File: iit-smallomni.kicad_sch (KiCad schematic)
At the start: 82 parts, among them J1 Battery, J10 DC-Motor, J2 HC_SR04, J3 HC_SR04, J4 HC_SR04, J5 DC-Motor, J6 DC-Motor, J7 DC-Motor, J8 DC-Motor, J9 DC-Motor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

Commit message: Change reset capacitor to 10uF
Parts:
- C1: value 10n -> 10u
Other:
- note added: "10uF to auto-reset when programming"
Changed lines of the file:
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@@
 		)
 	)
+	(text "10uF to auto-reset\nwhen programming"
+		(exclude_from_sim no)
+		(at 172.466 31.75 0)
+		(effects
+			(font
+				(size 1.27 1.27)
+			)
+		)
+	)
 	(text "MPU-9250 IMU"
 		(exclude_from_sim no)
@@
 			)
 		)
-		(property "Value" "10n"
+		(property "Value" "10u"
 			(at 173.99 44.45 0)
 			(effects

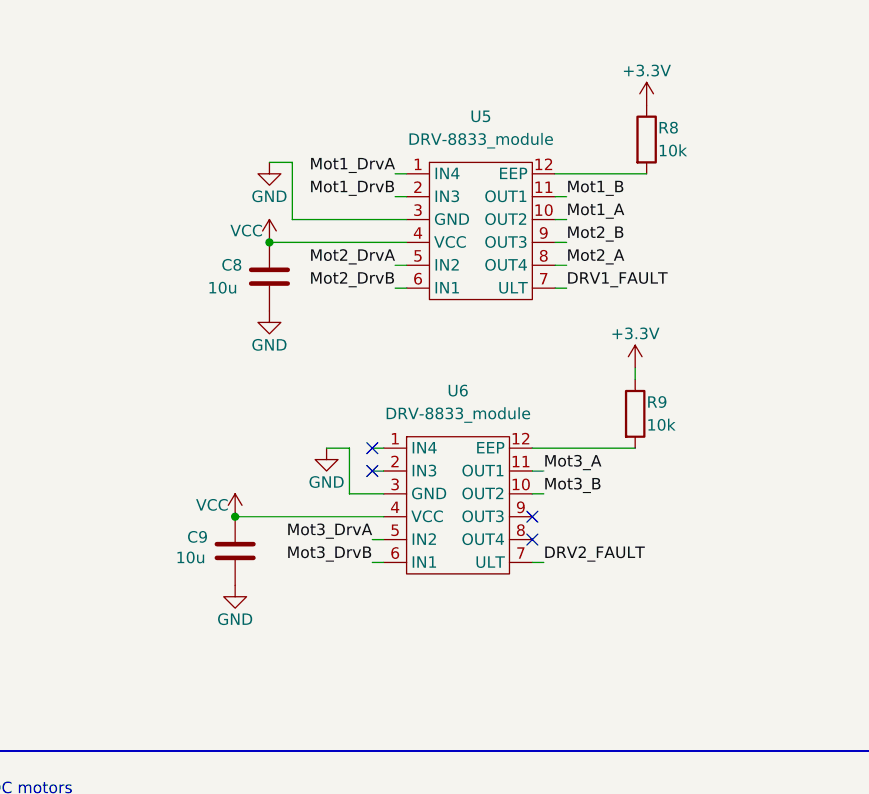
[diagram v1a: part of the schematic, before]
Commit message: Fix flipped DRV8833
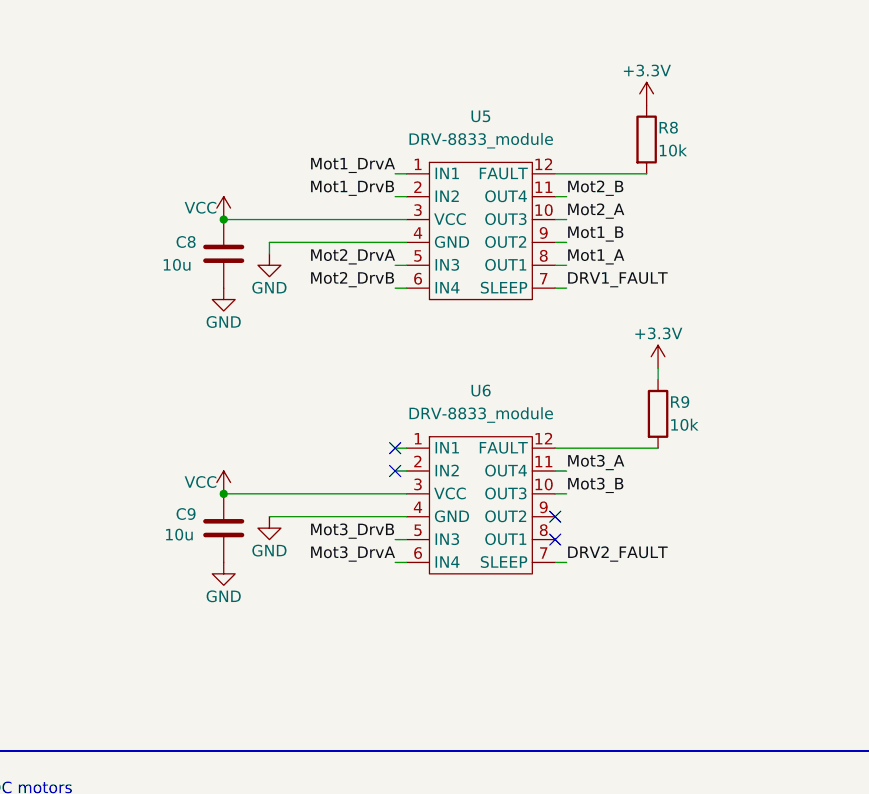
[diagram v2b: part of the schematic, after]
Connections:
- net GND: now also U5.4 (GND), U6.4 (GND); no longer U5.3 (GND), U6.3 (GND)
- net Mot1_A: now also U5.8 (OUT1); no longer U5.10 (OUT2)
- net Mot1_B: now also U5.9 (OUT2); no longer U5.11 (OUT1)
- net Mot2_A: now also U5.10 (OUT3); no longer U5.8 (OUT4)
- net Mot2_B: now also U5.11 (OUT4); no longer U5.9 (OUT3)
- net Mot3_DrvA: now also U6.6 (IN4); no longer U6.5 (IN2)
- net Mot3_DrvB: now also U6.5 (IN3); no longer U6.6 (IN1)
- net VCC: now also U5.3 (VCC), U6.3 (VCC); no longer U5.4 (VCC), U6.4 (VCC)
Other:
- moved on the sheet: C8, C9, R9, U6

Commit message: Fix flipped DSN-1504
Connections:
- net +5V: now also U2.4 (Output+); no longer U2.3 (Output+)
- net GND: now also U2.2 (Input-), U2.3 (Output-); no longer U2.1 (Input-), U2.4 (Output-)
- net Mot3_DrvA: now also U6.5 (IN3); no longer U6.6 (IN4)
- net Mot3_DrvB: now also U6.6 (IN4); no longer U6.5 (IN3)
- net at D1.1 (K): now also U2.1 (Input+); no longer U2.2 (Input+)
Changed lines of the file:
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@@
 	)
 	(label "Mot3_DrvB"
-		(at 351.79 80.01 180)
+		(at 351.79 82.55 180)
 		(fields_autoplaced yes)
 		(effects
@@
 	)
 	(label "Mot3_DrvA"
-		(at 351.79 82.55 180)
+		(at 351.79 80.01 180)
 		(fields_autoplaced yes)
 		(effects
@@
 		(lib_id "iit-smallomni:DSN-1504_module")
 		(at 90.17 26.67 0)
-		(mirror x)
 		(unit 1)
 		(exclude_from_sim no)
@@
 		(dnp no)
 		(property "Reference" "U2"
-			(at 90.17 22.606 0)
+			(at 90.17 22.86 0)
 			(effects
 				(font
@@
 		)
 		(property "Value" "DSN-1504_module"
-			(at 90.678 21.082 0)
+			(at 90.424 20.828 0)
 			(effects
 				(font
@@
 		)
 		(property "Footprint" "iit-smallomni:DSN1504_module"
-			(at 82.55 30.48 0)
+			(at 82.55 22.86 0)
 			(effects
 				(font
@@
 		)
 		(property "Datasheet" ""
-			(at 82.55 30.48 0)
+			(at 82.55 22.86 0)
 			(effects
 				(font

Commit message: Update Schottky diode footprint in design
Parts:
- D1: footprint Diode_SMD:D_0805_2012Metric_Pad1.15x1.40mm_HandSolder -> iit-smallomni:D_SOD-123FL
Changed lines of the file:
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@@
 			)
 		)
-		(property "Footprint" "Diode_SMD:D_0805_2012Metric_Pad1.15x1.40mm_HandSolder"
+		(property "Footprint" "iit-smallomni:D_SOD-123FL"
 			(at 73.66 25.4 0)
 			(effects

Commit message: Fix motor connector layout
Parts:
- J10, J8, J9: footprint iit-smallomni:motor -> iit-smallomni:legacy-motor
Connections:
- net +3.3V: now also J10.4 (Pin_4), J8.4 (Pin_4), J9.4 (Pin_4); no longer J10.5 (Pin_5), J8.5 (Pin_5), J9.5 (Pin_5)
- net GND: now also J10.3 (Pin_3), J8.3 (Pin_3), J9.3 (Pin_3); no longer J10.2 (Pin_2), J8.2 (Pin_2), J9.2 (Pin_2)
- net Mot1_B: now also J8.2 (Pin_2); no longer J8.6 (Pin_6)
- net Mot1_EncA: now also J8.5 (Pin_5); no longer J8.3 (Pin_3)
- net Mot1_EncB: now also J8.6 (Pin_6); no longer J8.4 (Pin_4)
- net Mot2_B: now also J9.2 (Pin_2); no longer J9.6 (Pin_6)
- net Mot2_EncA: now also J9.5 (Pin_5); no longer J9.3 (Pin_3)
- net Mot2_EncB: now also J9.6 (Pin_6); no longer J9.4 (Pin_4)
- net Mot3_B: now also J10.2 (Pin_2); no longer J10.6 (Pin_6)
- net Mot3_EncA: now also J10.5 (Pin_5); no longer J10.3 (Pin_3)
- net Mot3_EncB: now also J10.6 (Pin_6); no longer J10.4 (Pin_4)

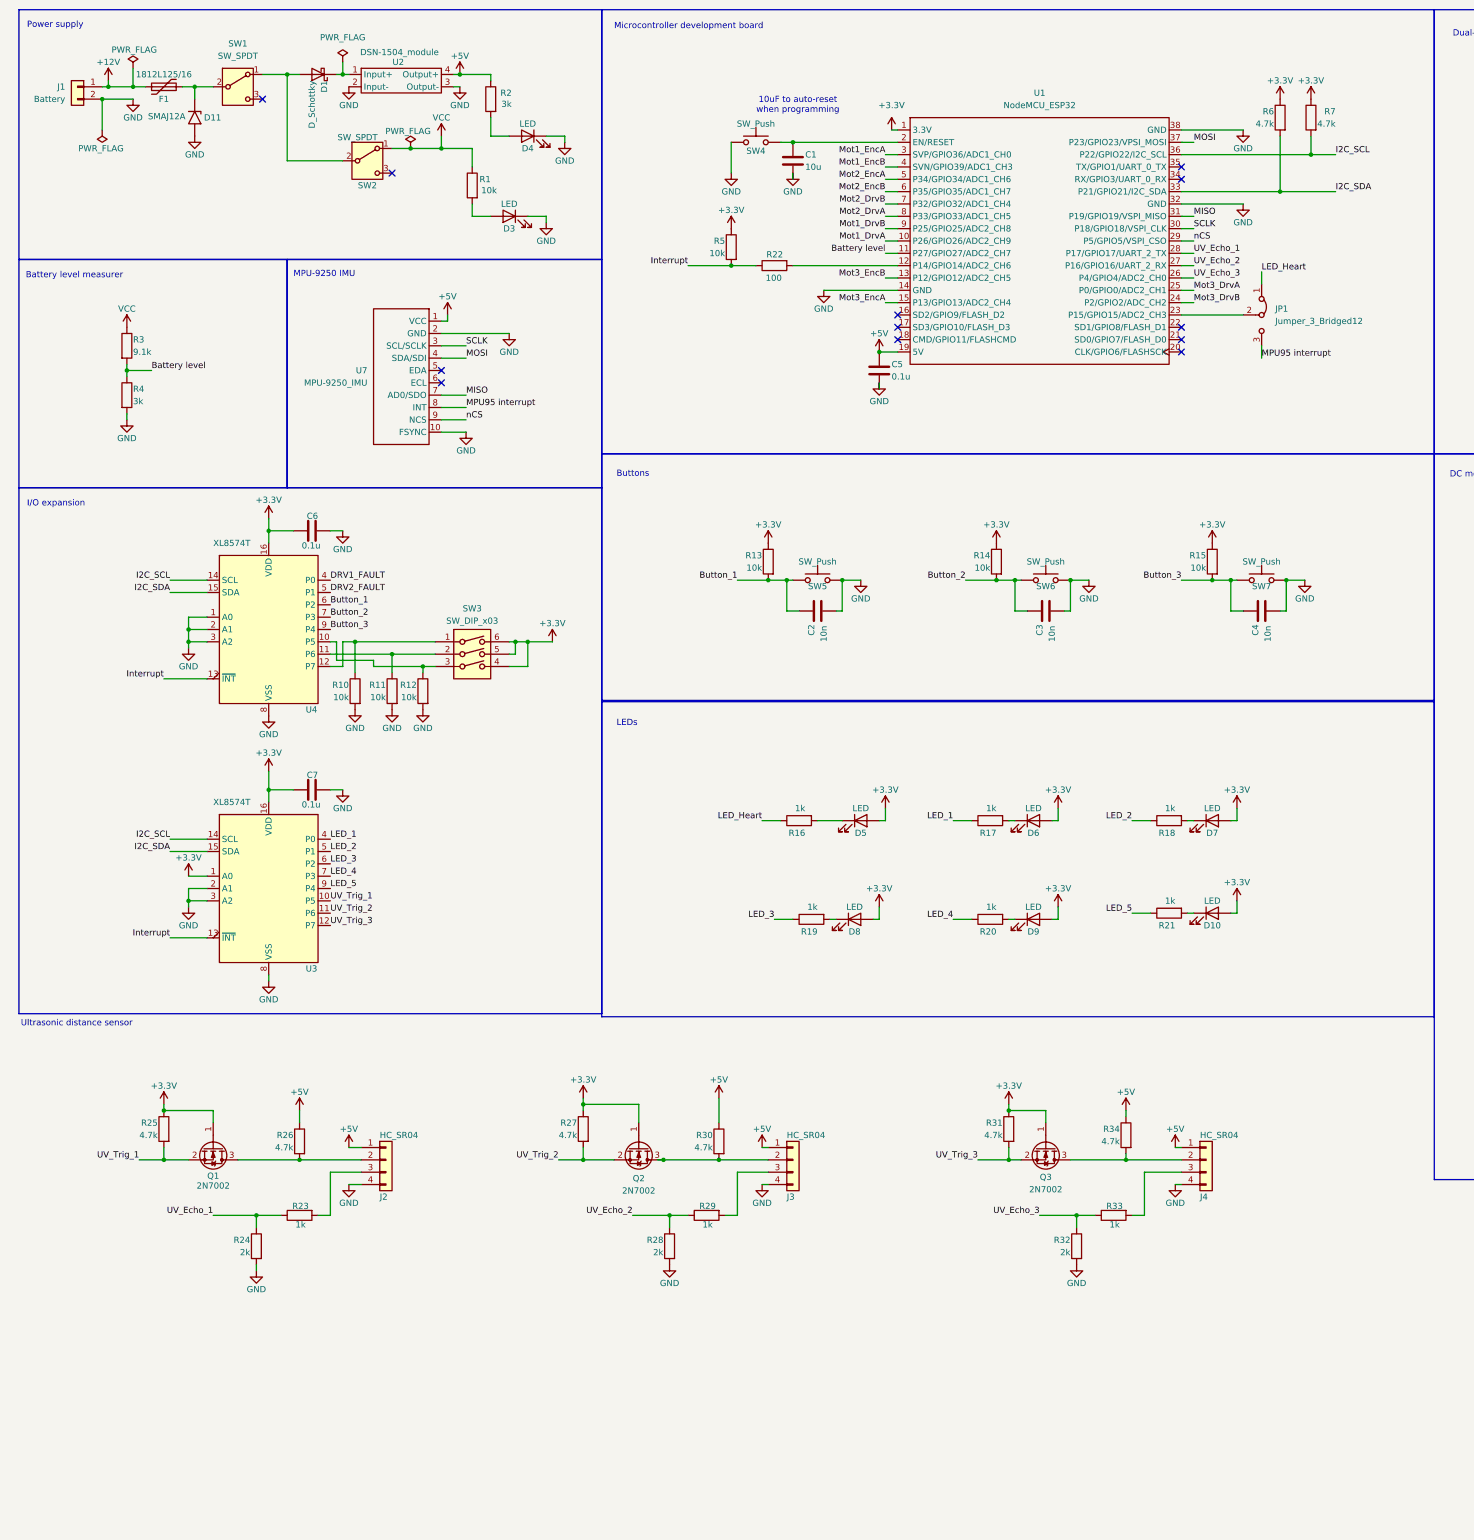
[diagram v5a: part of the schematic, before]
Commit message: JTAG, LiPo guard, Mounting hole
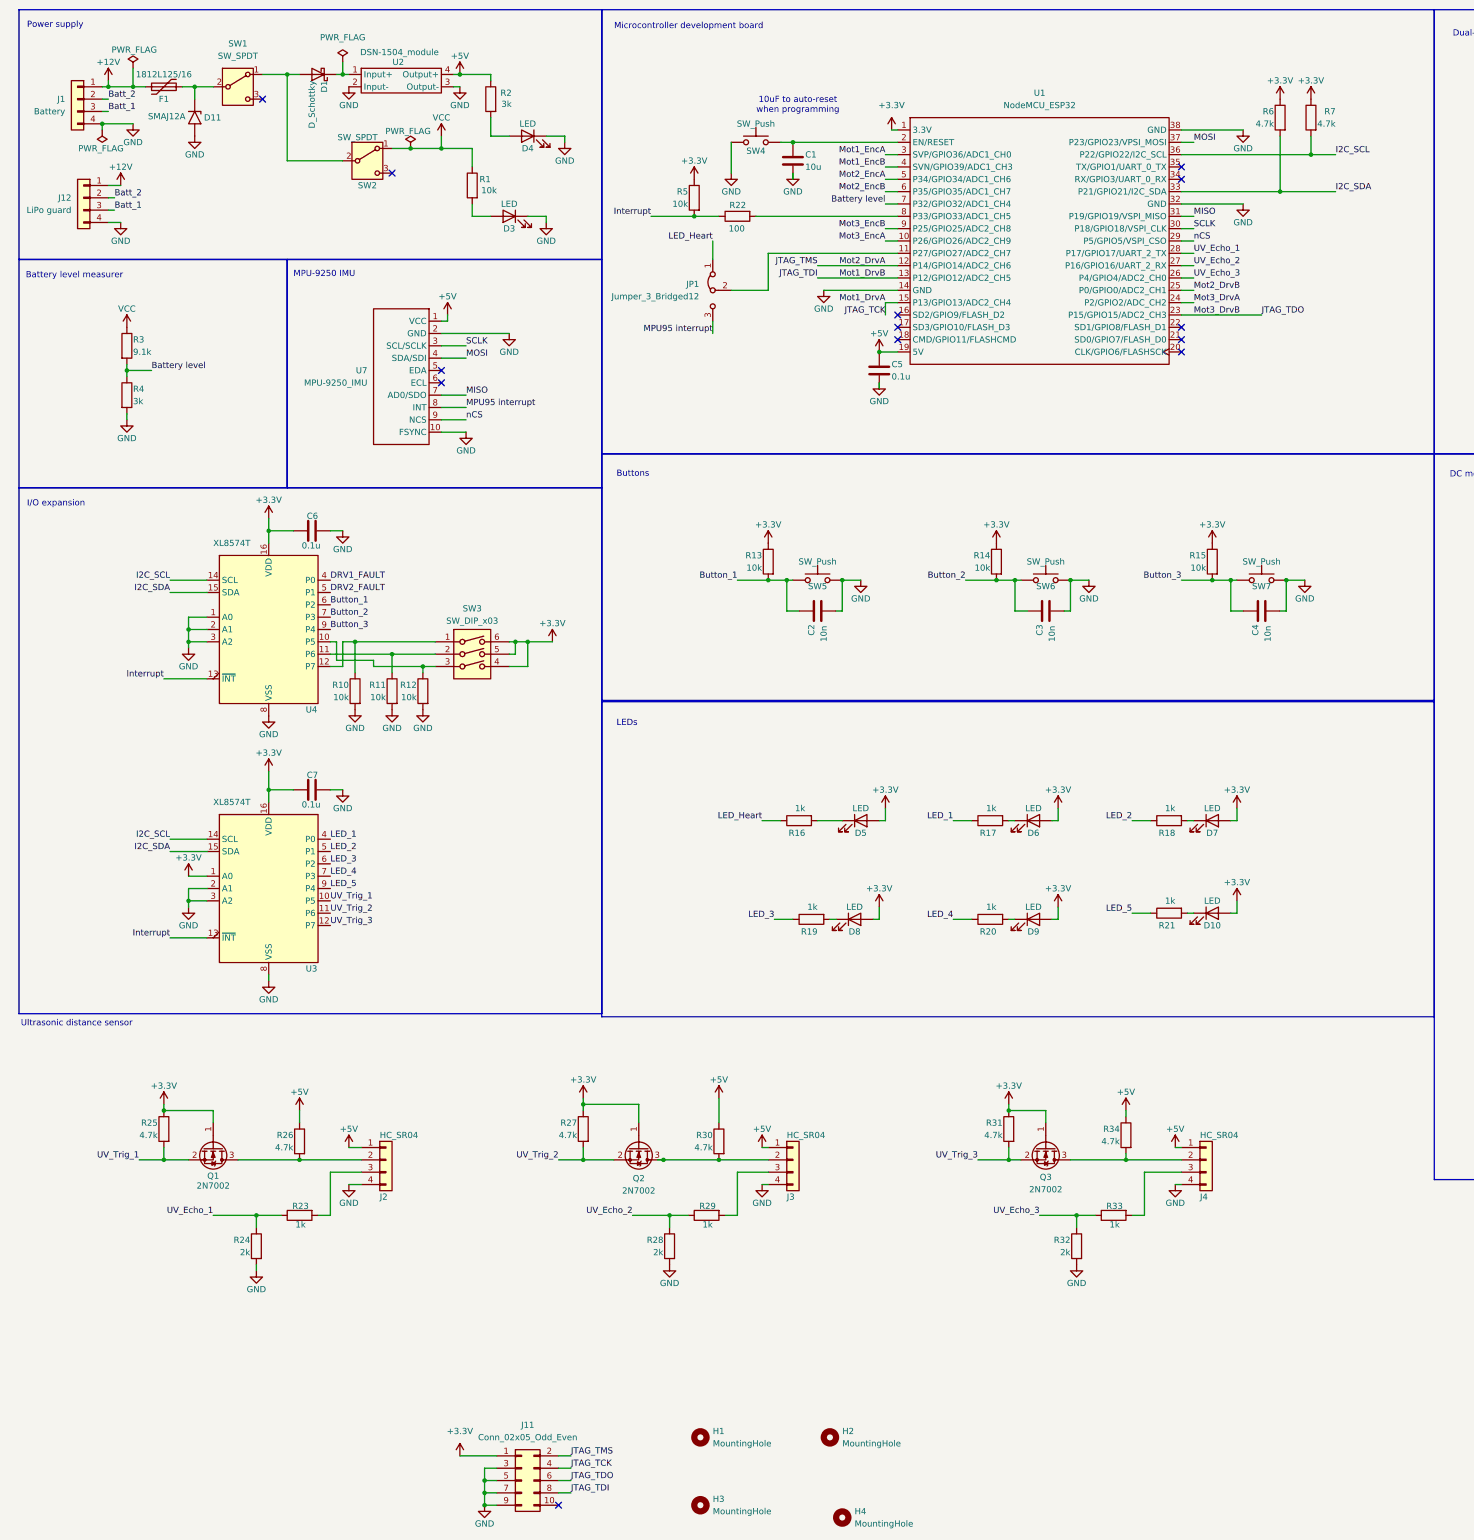
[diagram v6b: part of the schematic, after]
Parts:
- removed J1: Battery, Connector_Molex:Molex_KK-254_AE-6410-02A_1x02_P2.54mm_Vertical, symbol Connector_Generic:Conn_01x02
- added H1, H2, H3, H4: MountingHole, MountingHole:MountingHole_3.2mm_M3, symbol Mechanical:MountingHole
- added J1: Battery, Connector_Molex:Molex_KK-254_AE-6410-04A_1x04_P2.54mm_Vertical, symbol Connector_Generic:Conn_01x04
- added J11: Conn_02x05_Odd_Even, Connector_IDC:IDC-Header_2x05_P2.54mm_Vertical, symbol Connector_Generic:Conn_02x05_Odd_Even
- added J12: LiPo guard, Connector_PinSocket_2.54mm:PinSocket_1x04_P2.54mm_Vertical, symbol Connector_Generic:Conn_01x04
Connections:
- net +12V: now also J1.1 (Pin_1), J12.1 (Pin_1)
- net +3.3V: now also J11.1 (Pin_1)
- net Battery level: now also U1.7 (P32/GPIO32/ADC1_CH4); no longer U1.11 (P27/GPIO27/ADC2_CH7)
- net GND: now also J1.4 (Pin_4), J11.3 (Pin_3), J11.5 (Pin_5), J11.7 (Pin_7), J11.9 (Pin_9), J12.4 (Pin_4)
- net Mot2_DrvB: now also U1.25 (P0/GPIO0/ADC2_CH1); no longer U1.7 (P32/GPIO32/ADC1_CH4)
- net Mot3_DrvA: now also U1.24 (P2/GPIO2/ADC_CH2); no longer U1.25 (P0/GPIO0/ADC2_CH1)
- net Mot3_EncA: now also U1.10 (P26/GPIO26/ADC2_CH9); no longer U1.15 (P13/GPIO13/ADC2_CH4)
- net Mot3_EncB: now also U1.9 (P25/GPIO25/ADC2_CH8); no longer U1.13 (P12/GPIO12/ADC2_CH5)
- net at R22.2: now also U1.8 (P33/GPIO33/ADC1_CH5); no longer U1.12 (P14/GPIO14/ADC2_CH6)
- net at JP1.2 (C): now also U1.11 (P27/GPIO27/ADC2_CH7); no longer U1.23 (P15/GPIO15/ADC2_CH3)
- net Mot1_DrvA renamed JTAG_TCK
- net JTAG_TCK: now also U1.15 (P13/GPIO13/ADC2_CH4), J11.4 (Pin_4); no longer U1.10 (P26/GPIO26/ADC2_CH9)
- net Mot1_DrvB renamed JTAG_TDI
- net JTAG_TDI: now also U1.13 (P12/GPIO12/ADC2_CH5), J11.8 (Pin_8); no longer U1.9 (P25/GPIO25/ADC2_CH8)
- net Mot2_DrvA renamed JTAG_TMS
- net JTAG_TMS: now also U1.12 (P14/GPIO14/ADC2_CH6), J11.2 (Pin_2); no longer U1.8 (P33/GPIO33/ADC1_CH5)
- net Mot3_DrvB renamed JTAG_TDO
- net JTAG_TDO: now also U1.23 (P15/GPIO15/ADC2_CH3), J11.6 (Pin_6); no longer U1.24 (P2/GPIO2/ADC_CH2)
- new net Batt_1: J1.3 (Pin_3), J12.3 (Pin_3)
- new net Batt_2: J1.2 (Pin_2), J12.2 (Pin_2)
- no-connect marks 16 -> 17
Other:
- moved on the sheet: JP1, R22, R5

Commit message: Routing refinement around esp and i2c
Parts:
- JP1: footprint Connector:FanPinHeader_1x03_P2.54mm_Vertical -> Connector_PinHeader_2.54mm:PinHeader_1x03_P2.54mm_Vertical
- SW1, SW2: footprint Connector:FanPinHeader_1x03_P2.54mm_Vertical -> Connector_PinSocket_2.54mm:PinSocket_1x03_P2.54mm_Vertical
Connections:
- net Battery level: now also U1.6 (P35/GPIO35/ADC1_CH7); no longer U1.7 (P32/GPIO32/ADC1_CH4)
- net Button_1: now also U4.11 (P6); no longer U4.6 (P2)
- net Button_2: now also U4.10 (P5); no longer U4.7 (P3)
- net DRV1_FAULT: now also U5.12 (FAULT); no longer U5.7 (SLEEP)
- net DRV2_FAULT: now also U4.12 (P7), U6.12 (FAULT); no longer U4.5 (P1), U6.7 (SLEEP)
- net JTAG_TCK: now also U6.5 (IN3); no longer U5.1 (IN1)
- net JTAG_TDI: now also U6.2 (IN2); no longer U5.2 (IN2)
- net JTAG_TDO: now also U5.1 (IN1); no longer U6.6 (IN4)
- net JTAG_TMS: now also U6.1 (IN1); no longer U5.5 (IN3)
- net Mot1_EncA: now also U1.27 (P16/GPIO16/UART_2_RX); no longer U1.3 (SVP/GPIO36/ADC1_CH0)
- net Mot1_EncB: now also U1.26 (P4/GPIO4/ADC2_CH0); no longer U1.4 (SVN/GPIO39/ADC1_CH3)
- net Mot2_A: now also U6.9 (OUT2); no longer U5.10 (OUT3)
- net Mot2_B: now also U6.8 (OUT1); no longer U5.11 (OUT4)
- net Mot2_EncA: now also U1.4 (SVN/GPIO39/ADC1_CH3); no longer U1.5 (P34/GPIO34/ADC1_CH6)
- net Mot2_EncB: now also U1.3 (SVP/GPIO36/ADC1_CH0); no longer U1.6 (P35/GPIO35/ADC1_CH7)
- net Mot3_A: now also U6.10 (OUT3); no longer U6.11 (OUT4)
- net Mot3_B: now also U6.11 (OUT4); no longer U6.10 (OUT3)
- net Mot3_EncA: now also U1.8 (P33/GPIO33/ADC1_CH5); no longer U1.10 (P26/GPIO26/ADC2_CH9)
- net Mot3_EncB: now also U1.7 (P32/GPIO32/ADC1_CH4); no longer U1.9 (P25/GPIO25/ADC2_CH8)
- net UV_Echo_1: now also U1.11 (P27/GPIO27/ADC2_CH7); no longer U1.28 (P17/GPIO17/UART_2_TX)
- net UV_Echo_2: now also U1.24 (P2/GPIO2/ADC_CH2); no longer U1.27 (P16/GPIO16/UART_2_RX)
- net UV_Echo_3: now also U1.5 (P34/GPIO34/ADC1_CH6); no longer U1.26 (P4/GPIO4/ADC2_CH0)
- net at JP1.2 (C): now also U1.9 (P25/GPIO25/ADC2_CH8); no longer U1.11 (P27/GPIO27/ADC2_CH7)
- net at R22.2: now also U1.10 (P26/GPIO26/ADC2_CH9); no longer U1.8 (P33/GPIO33/ADC1_CH5)
- net at R12.1, SW3.3: now also U4.7 (P3); no longer U4.10 (P5)
- net at R8.2: now also U5.7 (SLEEP); no longer U5.12 (FAULT)
- net at R10.1, SW3.1: now also U4.5 (P1); no longer U4.12 (P7)
- net at R11.1, SW3.2: now also U4.6 (P2); no longer U4.11 (P6)
- net at R9.2: now also U6.7 (SLEEP); no longer U6.12 (FAULT)
- net Mot2_DrvB: no longer names the net of U5.6 (IN4)
- net Mot2_DrvB: no longer U1.25 (P0/GPIO0/ADC2_CH1)
- removed net Mot3_DrvA: U1.24 (P2/GPIO2/ADC_CH2), U6.5 (IN3)
- new net Mot1_DrvB: U1.25 (P0/GPIO0/ADC2_CH1), U5.2 (IN2)
- new net Mot3_DrvB: U1.28 (P17/GPIO17/UART_2_TX), U6.6 (IN4)
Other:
- moved on the sheet: R10, R11, R12, R8, R9, SW3
